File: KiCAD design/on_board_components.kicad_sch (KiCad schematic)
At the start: 9 parts, among them U401 ACS712xLCTR-20A

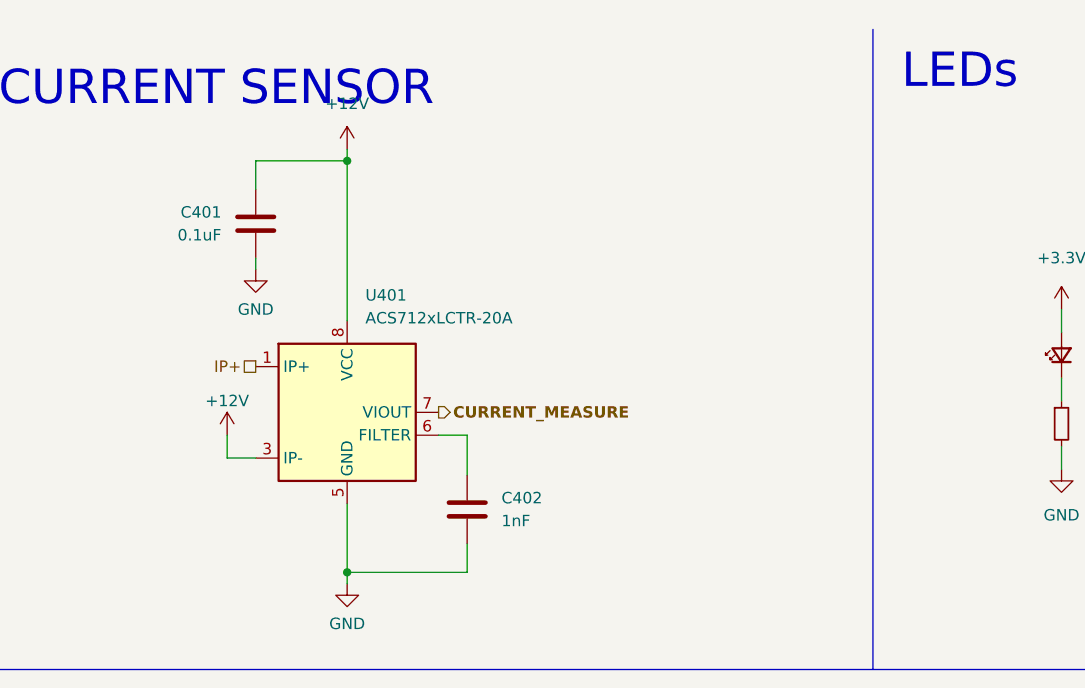
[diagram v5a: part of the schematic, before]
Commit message: voltage divider for current sensor
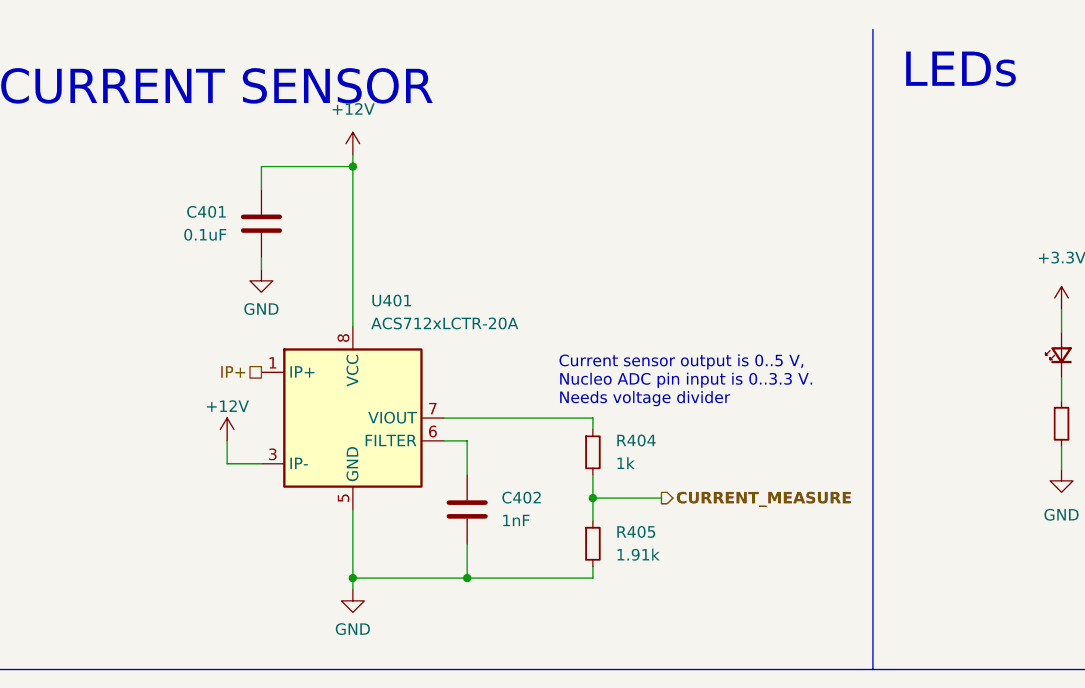
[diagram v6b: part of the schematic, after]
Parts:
- added R404: 1k, Resistor_SMD:R_0603_1608Metric_Pad0.98x0.95mm_HandSolder, symbol Device:R_Small
- added R405: 1.91k, Resistor_SMD:R_0603_1608Metric_Pad0.98x0.95mm_HandSolder, symbol Device:R_Small
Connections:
- net CURRENT_MEASURE: now also R404.2, R405.1; no longer U401.7 (VIOUT)
- net GND: now also R405.2
- new net: R404.1, U401.7 (VIOUT)
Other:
- note added: "Current sensor output is 0..5 V, Nucleo ADC pin input is 0..3.3 V. Needs voltage divider"
- moved on the sheet: C401, U401

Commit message: add purchase location (field PurchaseLoc) and price (field Price) to some main components, adding rest later
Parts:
- U401: Price (none) -> 4.01; PurchaseLoc (none) -> https://www.digikey.fi/en/products/detail/allegro-microsyst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
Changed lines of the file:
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@@
+      (effects (font (size 1.27 1.27)) hide)
+    )
+    (property "PurchaseLoc" "https://www.digikey.fi/en/products/detail/allegro-microsystems/ACS712ELCTR-20A-T/1284594" (id 4) (at 54.61 57.15 0)
+      (effects (font (size 1.27 1.27)) hide)
+    )
+    (property "Price" "4.01" (id 5) (at 54.61 57.15 0)
       (effects (font (size 1.27 1.27)) hide)
     )

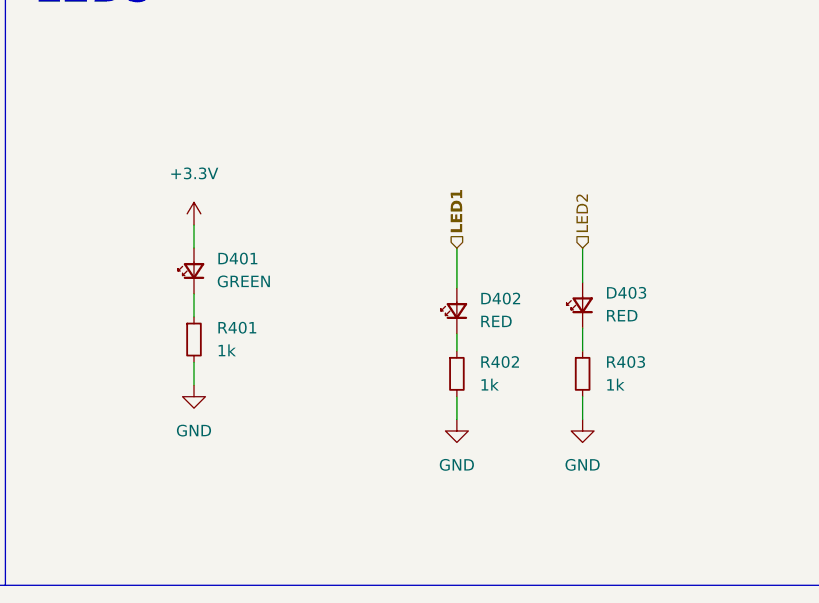
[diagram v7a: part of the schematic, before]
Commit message: Added LEDs
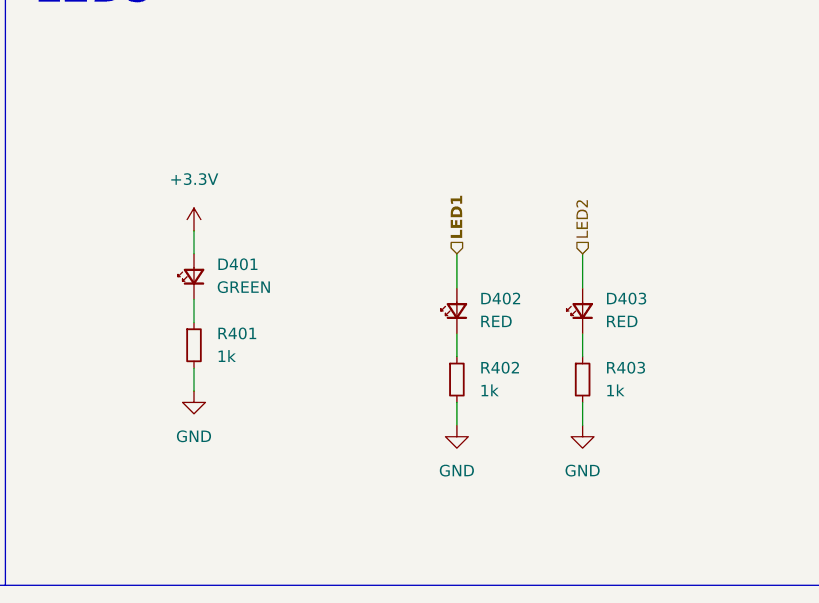
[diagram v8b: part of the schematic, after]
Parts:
- D401: footprint LED_SMD:LED_0603_1608Metric_Pad1.05x0.95mm_HandSolder -> LED_SMD:LED_1206_3216Metric; Price (none) -> 0,35; PurchaseLoc (none) -> https://www.digikey.fi/fi/products/detail/lumex-opto-compon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
- D402, D403: footprint LED_SMD:LED_0603_1608Metric_Pad1.05x0.95mm_HandSolder -> LED_SMD:LED_1206_3216Metric; Price (none) -> 0,36; PurchaseLoc (none) -> https://www.digikey.fi/fi/products/detail/lumex-opto-compon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
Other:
- moved on the sheet: D401, D403, R401, R402, R403
